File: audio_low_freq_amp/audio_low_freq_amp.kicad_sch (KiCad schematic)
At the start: 53 parts, among them Q1 PNP, Q10 NPN, Q11 PNP, Q12 NPN, Q13 PNP, Q2 PNP, Q3 NPN, Q4 NPN, Q5 PNP, Q6 NPN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

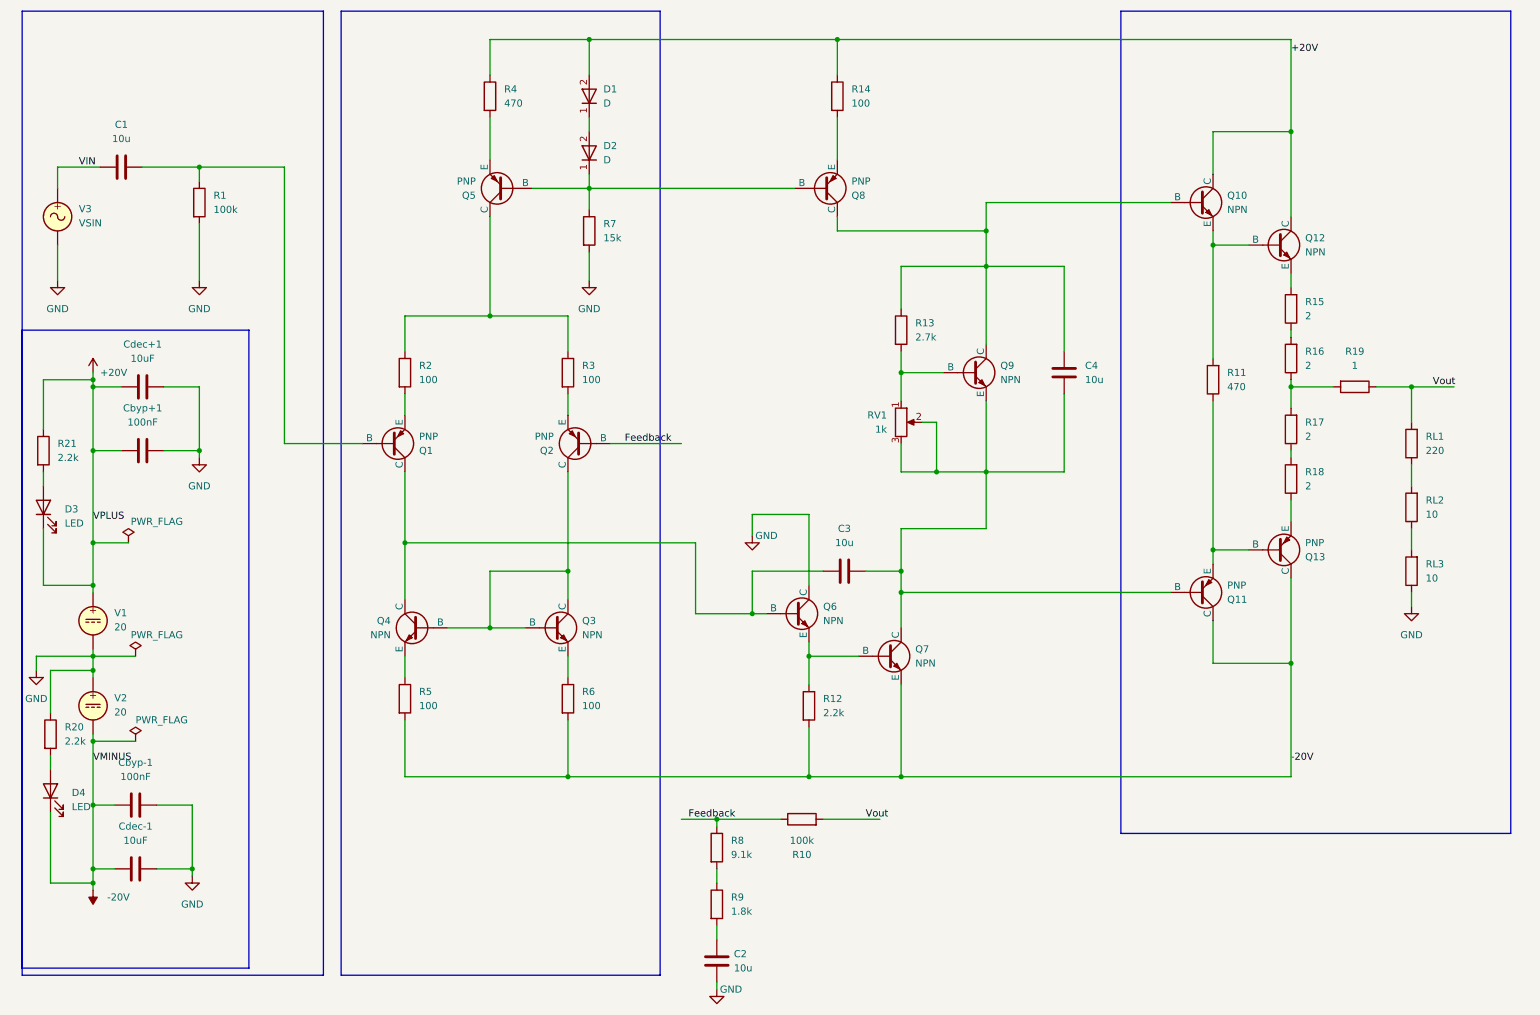
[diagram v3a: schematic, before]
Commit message: added constraints to pcb and did some custom footprints
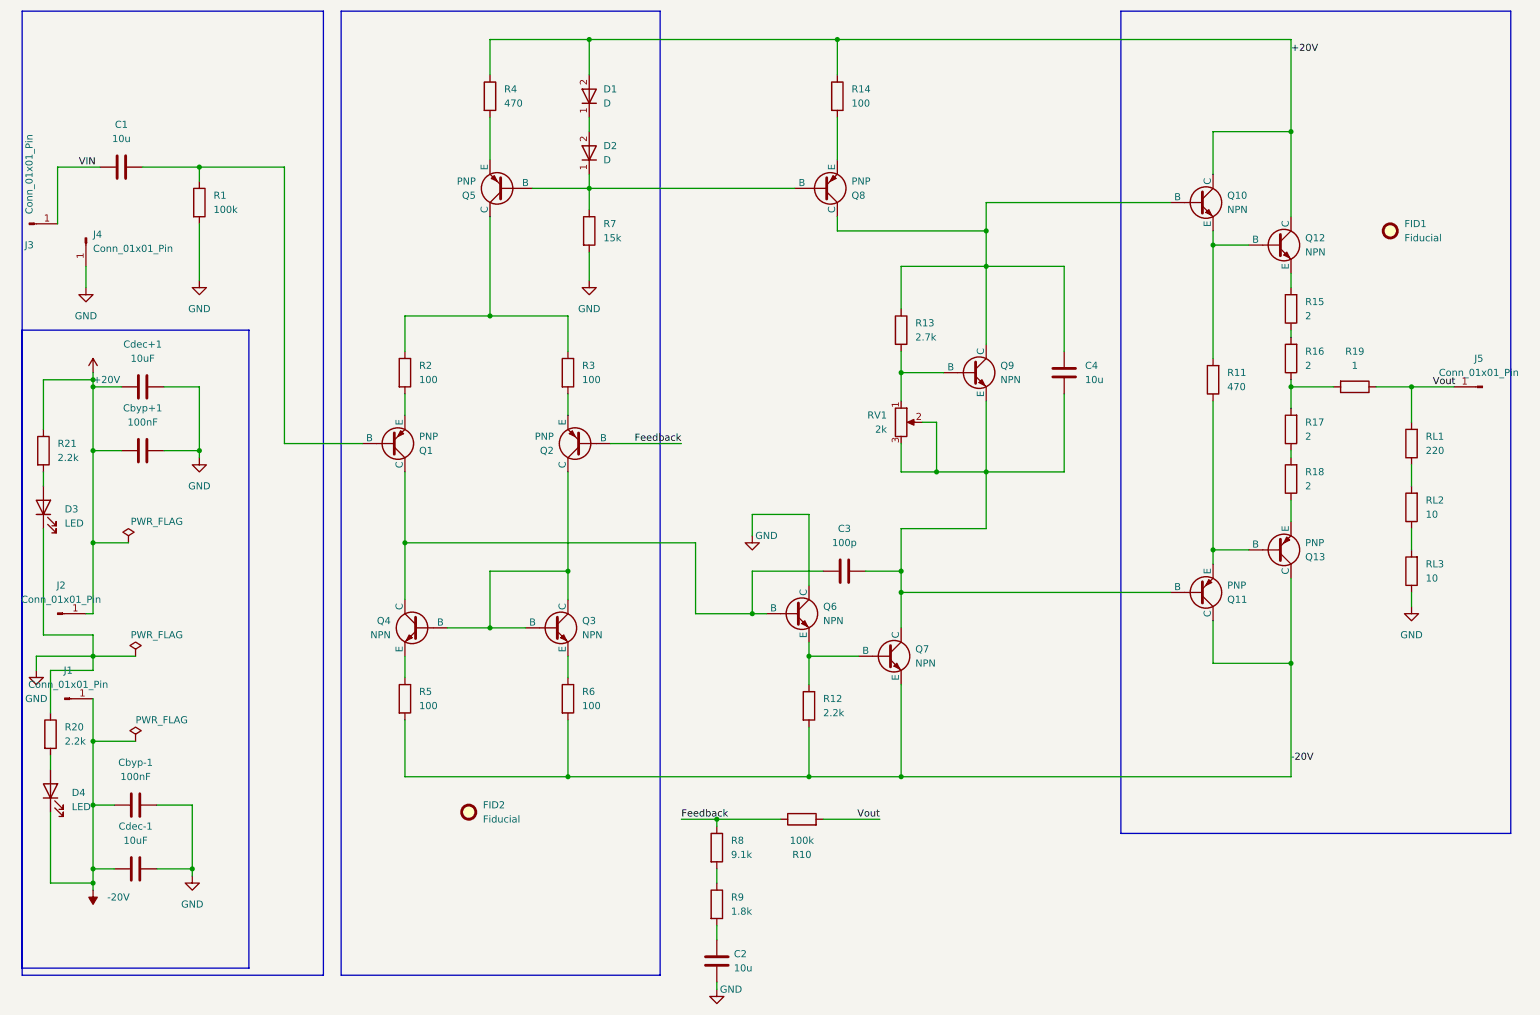
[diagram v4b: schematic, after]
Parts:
- removed V1, V2: 20, symbol Simulation_SPICE:VDC
- removed V3: VSIN, symbol Simulation_SPICE:VSIN
- added FID1, FID2: Fiducial, Fiducial:Fiducial_1mm_Mask2mm, symbol Mechanical:Fiducial
- added J1, J2, J3, J4, J5: Conn_01x01_Pin, my_lib_Radu:J_conn_4x4mm_Radu, symbol Connector:Conn_01x01_Pin
- C1, C2, C4, Cdec+1, Cdec-1: footprint (none) -> my_lib_Radu:10uF_smd_6.3x5.4_Radu
- C3: value 10u -> 100p; footprint (none) -> Capacitor_SMD:C_0805_2012Metric
- Cbyp+1, Cbyp-1: footprint (none) -> Capacitor_SMD:C_0805_2012Metric
- D1, D2: footprint (none) -> Diode_SMD:D_0805_2012Metric
- Q1, Q10, Q11, Q12, Q13, Q2, Q3, Q4, Q5, Q6, Q7, Q8, Q9: footprint (none) -> my_lib_Radu:sot23_Radu
- RL1, RL2, RL3: footprint (none) -> Resistor_SMD:R_0805_2012Metric
- RV1: value 1k -> 2k; footprint Potentiometer_SMD:Potentiometer_Vishay_TS53YL_Vertical -> my_lib_Radu:ts53yl_Radu
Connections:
- net +20V: now also J2.1 (Pin_1); no longer D3.1 (K)
- net -20V: now also J1.1 (Pin_1)
- net GND: now also D3.1 (K), J4.1 (Pin_1)
- net VIN: now also J3.1 (Pin_1)
- net Vout: now also J5.1 (Pin_1)

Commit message: layed out the parts on pcb, next is routing
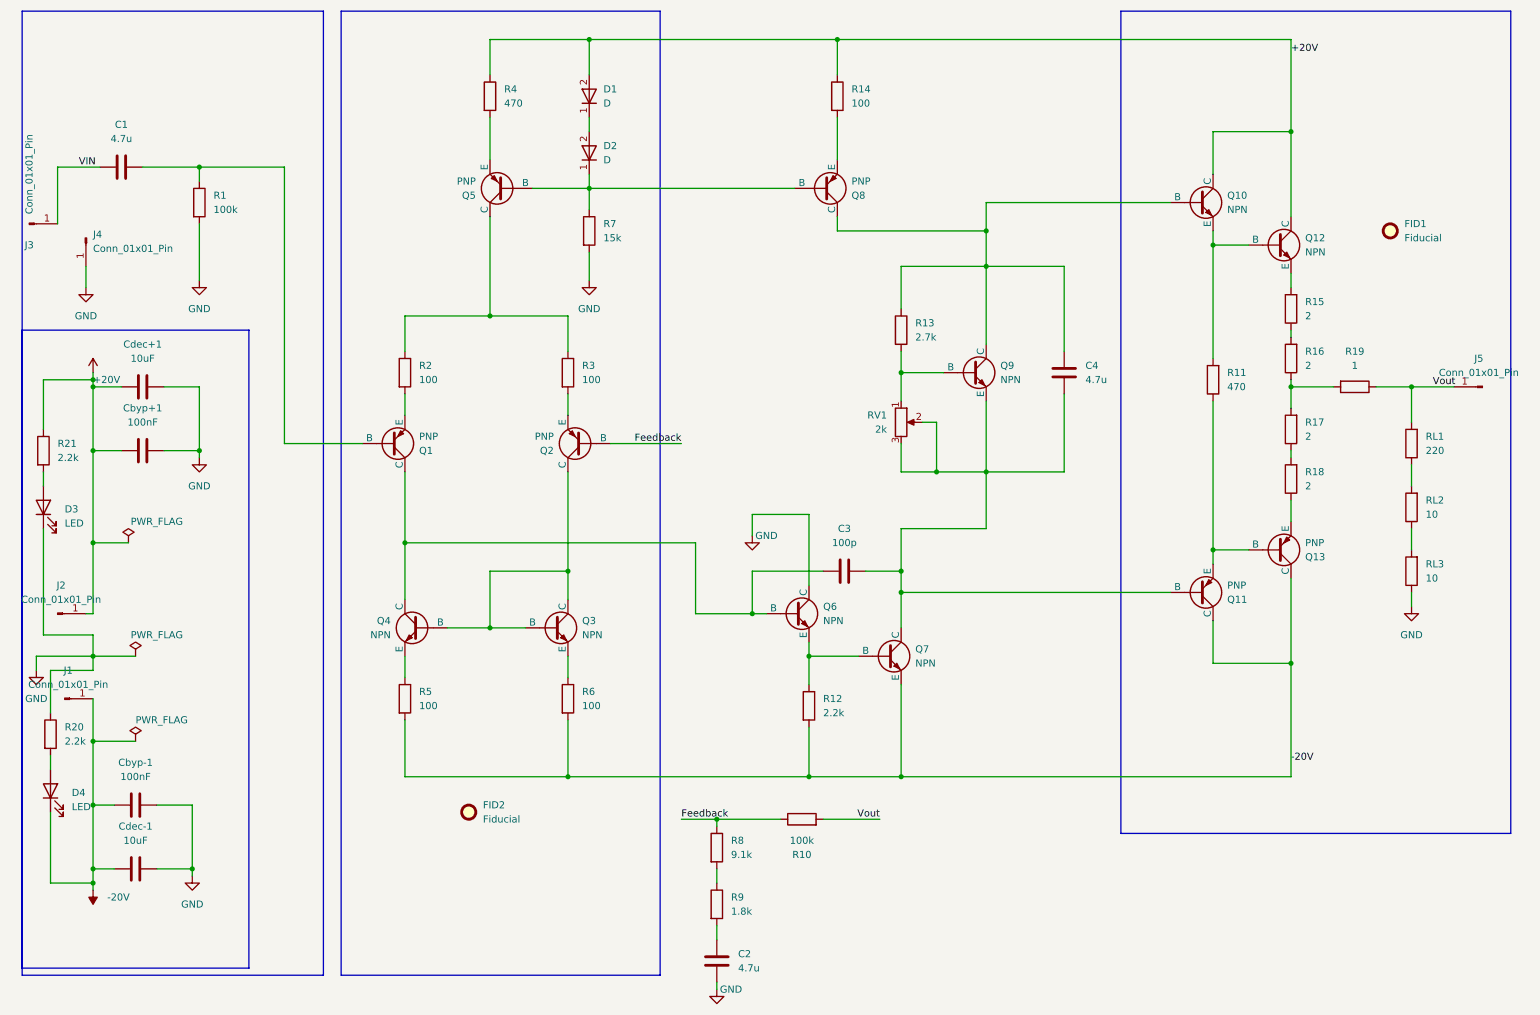
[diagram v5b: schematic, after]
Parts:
- C1, C2, C4: value 10u -> 4.7u; footprint my_lib_Radu:10uF_smd_6.3x5.4_Radu -> Capacitor_SMD:C_0805_2012Metric
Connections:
- net -20V: now also Cdec-1.2; no longer Cdec-1.1
- net GND: now also Cdec-1.1; no longer Cdec-1.2
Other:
- moved on the sheet: Cdec-1
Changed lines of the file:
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@@
 	)
 	(junction
+		(at 44.45 172.72)
+		(diameter 0)
+		(color 0 0 0 0)
+	)
+	(junction
 		(at 45.72 97.79)
 		(diameter 0)
@@
 	)
 	(junction
-		(at 44.45 172.72)
-		(diameter 0)
-		(color 0 0 0 0)
-	)
-	(junction
 		(at 26.67 172.72)
 		(diameter 0)
@@
 	(wire
 		(pts
-			(xy 44.45 161.29) (xy 44.45 172.72)
-		)
-		(stroke
-			(width 0)
-			(type default)
-		)
-	)
-	(wire
-		(pts
 			(xy 241.3 40.64) (xy 241.3 55.88)
 		)
@@
 	(wire
 		(pts
+			(xy 26.67 172.72) (xy 26.67 175.26)
+		)
+		(stroke
+			(width 0)
+			(type default)
+		)
+	)
+	(wire
+		(pts
 			(xy 82.55 134.62) (xy 82.55 138.43)
 		)
@@
 	(wire
 		(pts
+			(xy 44.45 172.72) (xy 44.45 173.99)
+		)
+		(stroke
+			(width 0)
+			(type default)
+		)
+	)
+	(wire
+		(pts
 			(xy 256.54 86.36) (xy 262.89 86.36)
 		)
@@
 	(wire
 		(pts
-			(xy 44.45 173.99) (xy 44.45 172.72)
+			(xy 138.43 193.04) (xy 138.43 194.31)
 		)
 		(stroke
@@
 	(wire
 		(pts
-			(xy 138.43 193.04) (xy 138.43 194.31)
+			(xy 115.57 24.13) (xy 115.57 30.48)
 		)
 		(stroke
@@
 	(wire
 		(pts
-			(xy 115.57 24.13) (xy 115.57 30.48)
+			(xy 97.79 119.38) (xy 111.76 119.38)
 		)
 		(stroke
@@
 	(wire
 		(pts
-			(xy 97.79 119.38) (xy 111.76 119.38)
+			(xy 60.96 96.52) (xy 74.93 96.52)
 		)
 		(stroke
@@
 	(wire
 		(pts
-			(xy 60.96 96.52) (xy 74.93 96.52)
+			(xy 26.67 161.29) (xy 26.67 172.72)
 		)
 		(stroke
@@
 	(wire
 		(pts
-			(xy 26.67 172.72) (xy 26.67 175.26)
+			(xy 90.17 129.54) (xy 97.79 129.54)
 		)
 		(stroke
@@
 	(wire
 		(pts
-			(xy 90.17 129.54) (xy 97.79 129.54)
+			(xy 44.45 161.29) (xy 44.45 172.72)
 		)
 		(stroke
@@
 	(wire
 		(pts
-			(xy 26.67 161.29) (xy 26.67 172.72)
-		)
-		(stroke
-			(width 0)
-			(type default)
-		)
-	)
-	(wire
-		(pts
 			(xy 111.76 134.62) (xy 111.76 138.43)
 		)
@@
 		(fields_autoplaced yes)
 		(property "Reference" "C2"
-			(at 141.486 187.9599 0)
+			(at 142.24 187.9599 0)
 			(effects
 				(font
@@
 			)
 		)
-		(property "Value" "10u"
-			(at 141.486 190.4999 0)
+		(property "Value" "4.7u"
+			(at 142.24 190.4999 0)
 			(effects
 				(font
@@
 			)
 		)
-		(property "Footprint" "my_lib_Radu:10uF_smd_6.3x5.4_Radu"
+		(property "Footprint" "Capacitor_SMD:C_0805_2012Metric"
 			(at 137.4648 185.42 0)
 			(effects
@@
 	(symbol
 		(lib_id "Device:C")
-		(at 34.29 172.72 90)
+		(at 34.29 172.72 270)
 		(unit 1)
 		(exclude_from_sim no)
@@
 		)
 		(property "Footprint" "my_lib_Radu:10uF_smd_6.3x5.4_Radu"
-			(at 38.1 171.7548 0)
+			(at 30.48 173.6852 0)
 			(effects
 				(font
@@
 		(fields_autoplaced yes)
 		(property "Reference" "C4"
-			(at 204.4002 82.5499 0)
+			(at 204.47 82.5499 0)
 			(effects
 				(font
@@
 			)
 		)
-		(property "Value" "10u"
-			(at 204.4002 85.0899 0)
+		(property "Value" "4.7u"
+			(at 204.47 85.0899 0)
 			(effects
 				(font
@@
 			)
 		)
-		(property "Footprint" "my_lib_Radu:10uF_smd_6.3x5.4_Radu"
+		(property "Footprint" "Capacitor_SMD:C_0805_2012Metric"
 			(at 199.6948 80.01 0)
 			(effects
@@
 			)
 		)
-		(property "Value" "10u"
+		(property "Value" "4.7u"
 			(at 31.75 41.91 90)
 			(effects
@@
 			)
 		)
-		(property "Footprint" "my_lib_Radu:10uF_smd_6.3x5.4_Radu"
+		(property "Footprint" "Capacitor_SMD:C_0805_2012Metric"
 			(at 35.56 46.0248 0)
 			(effects
